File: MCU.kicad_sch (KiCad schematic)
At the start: 12 parts, among them J1 Conn_ARM_SWD_TagConnect_TC203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, SW1 SW_000001, SW2 SW_000001, U1 NORA-B106-00B, Y1 CLK_0003

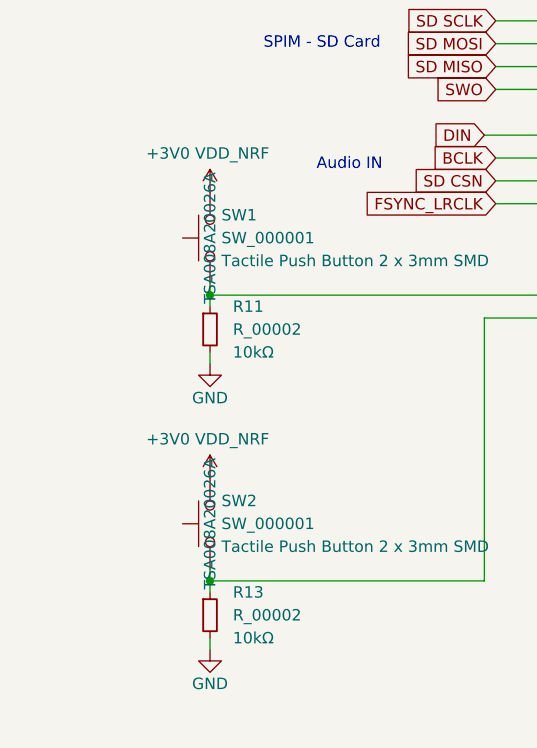
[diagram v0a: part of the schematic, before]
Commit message: fixed SD card footprintg
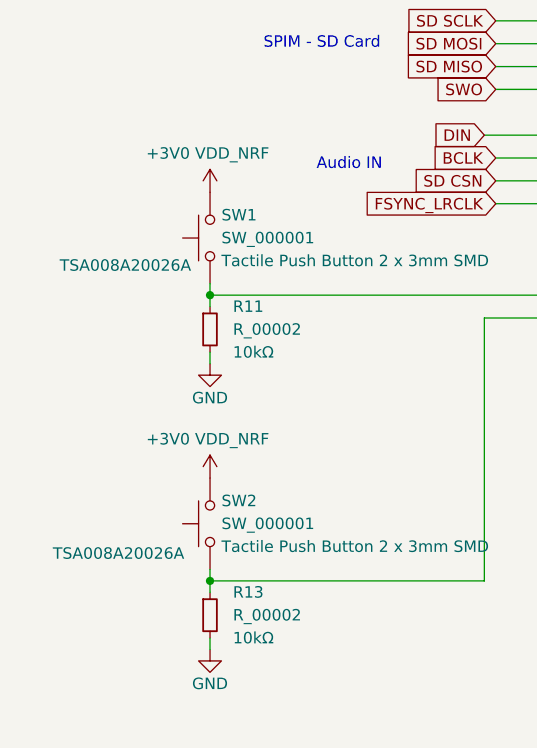
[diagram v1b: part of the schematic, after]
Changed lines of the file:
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@@
 		(on_board yes)
 		(dnp no)
-		(fields_autoplaced yes)
 		(property "Reference" "SW1"
 			(at 49.53 120.6499 90)
@@
 		)
 		(property "MPNs" "TSA008A20026A "
-			(at 48.26 123.19 0)
+			(at 38.862 126.238 90)
 			(effects
 				(font
@@
 		(on_board yes)
 		(dnp no)
-		(fields_autoplaced yes)
 		(property "Reference" "SW2"
 			(at 49.53 152.3999 90)
@@
 		)
 		(property "MPNs" "TSA008A20026A "
-			(at 48.26 154.94 0)
-			(effects
-				(font
+			(at 38.1 158.242 90)
+			(effects
+				(font

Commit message: added test points
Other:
- note removed: "Debug Voltage level Considerations!"
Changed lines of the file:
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@@
-		)
-	)
-	(text "Debug Voltage level Considerations!"
-		(exclude_from_sim no)
-		(at 48.26 21.082 0)
-		(effects
-			(font
-				(size 1.27 1.27)
-			)
 		)
 	)

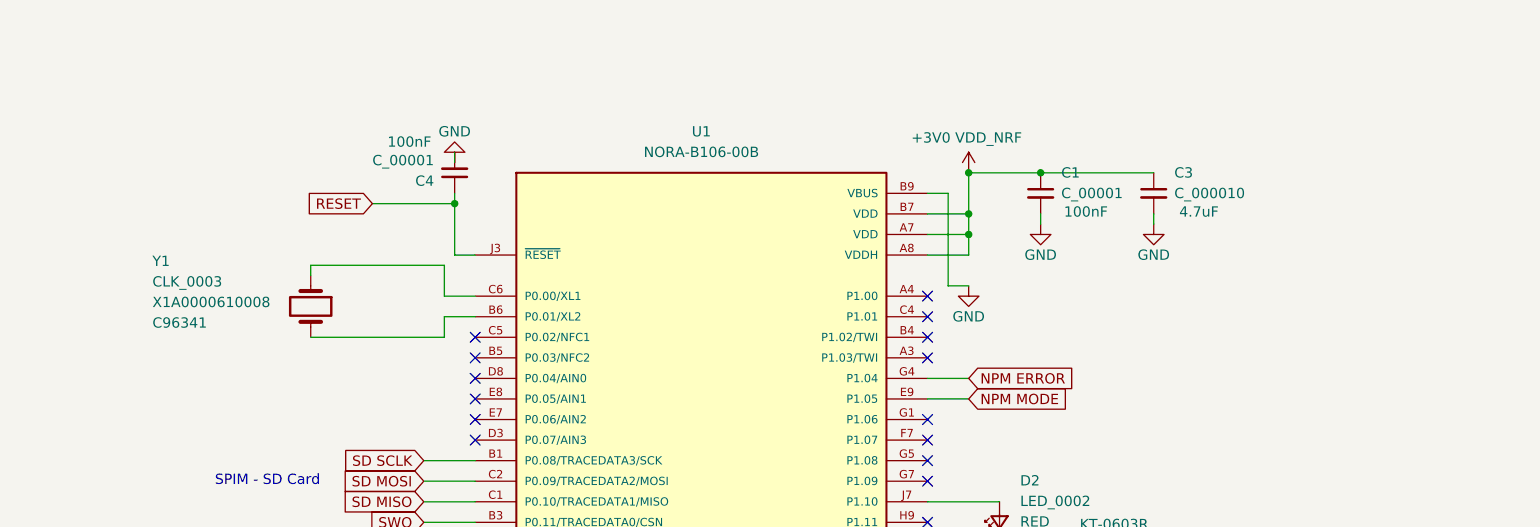
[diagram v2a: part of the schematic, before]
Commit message: added additional decoupling capacitors
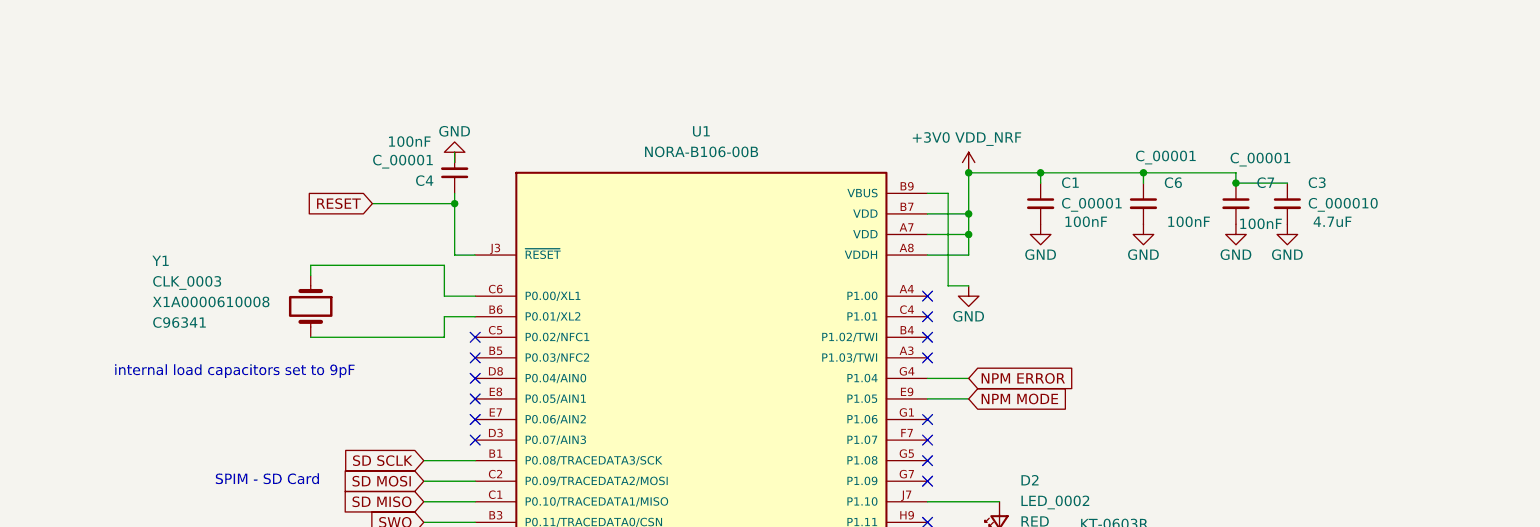
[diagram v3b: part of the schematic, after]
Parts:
- added C6, C7: C_00001, Capacitor_SMD:C_0402_1005Metric, symbol mic_patch_parts:C_00001
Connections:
- net +3V0 VDD_NRF: now also C6.1, C7.1
- net GND: now also C6.2, C7.2
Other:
- note added: "internal load capacitors set to 9pF"
- moved on the sheet: C1, C3

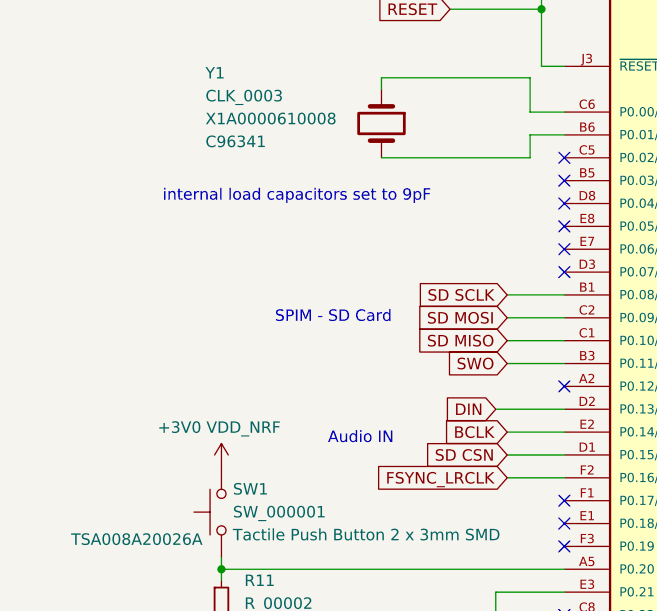
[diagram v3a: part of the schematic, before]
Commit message: fixed ERC errors
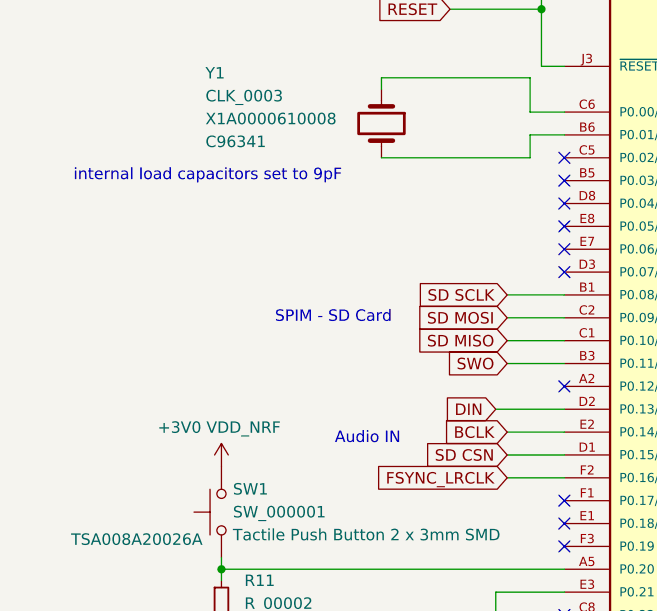
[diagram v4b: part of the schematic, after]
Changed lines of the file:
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@@
 	(text "internal load capacitors set to 9pF"
 		(exclude_from_sim no)
-		(at 56.642 88.138 0)
+		(at 46.736 85.852 0)
 		(effects
 			(font
@@
 	(text "Audio IN"
 		(exclude_from_sim no)
-		(at 63.754 115.062 0)
+		(at 64.516 115.062 0)
 		(effects
 			(font

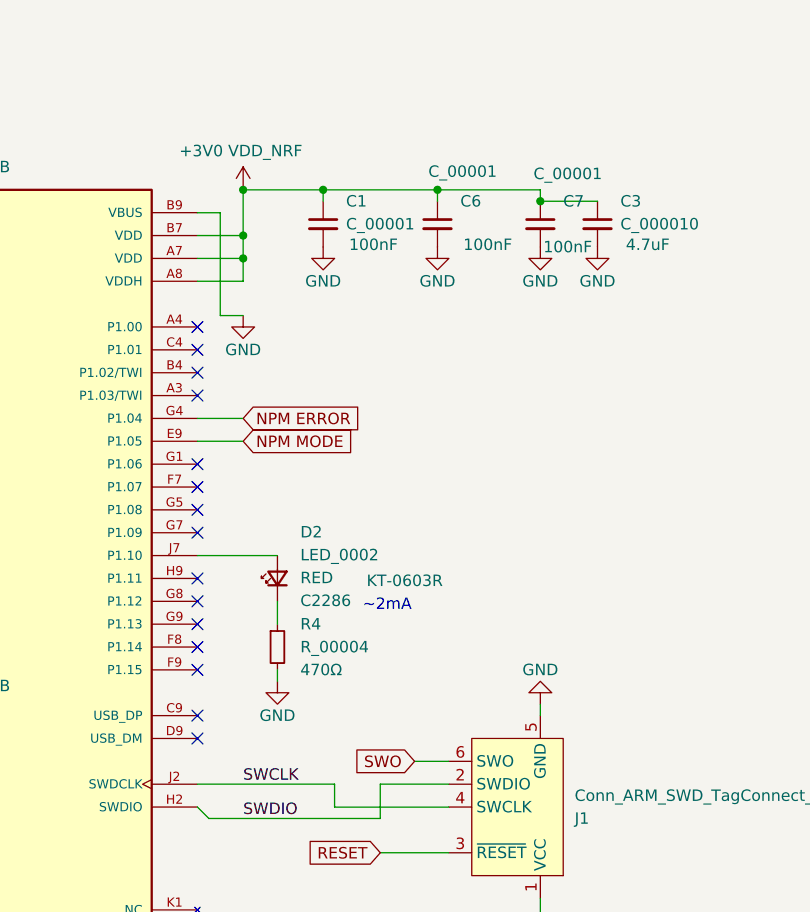
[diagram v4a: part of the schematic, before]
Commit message: switched around pins for easier routing
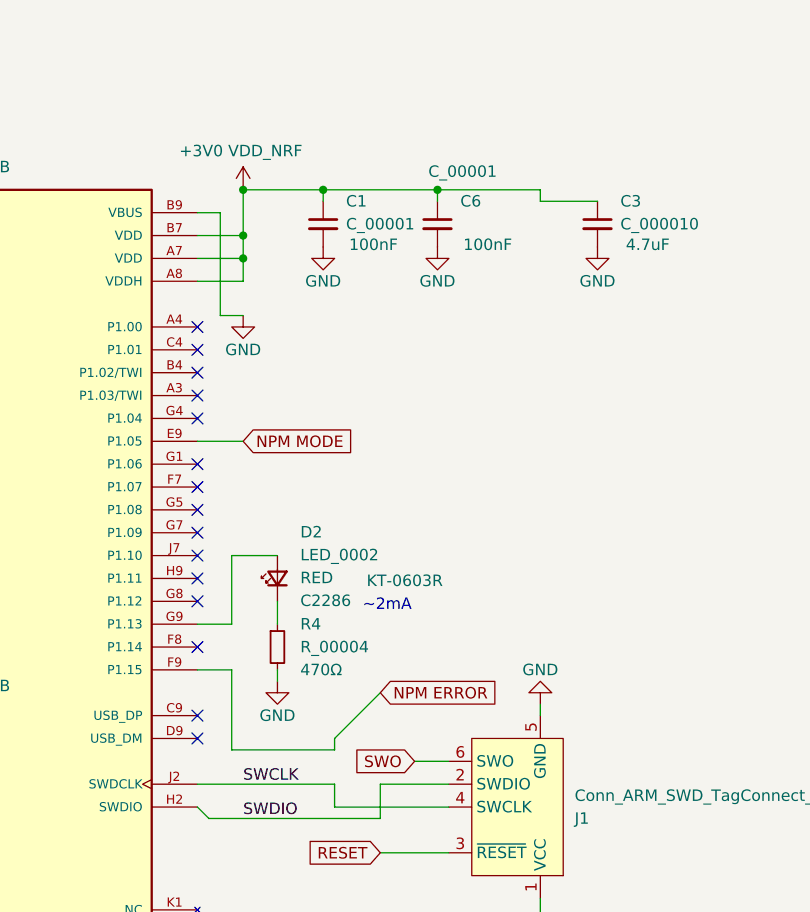
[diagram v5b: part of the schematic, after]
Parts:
- removed C7: C_00001, Capacitor_SMD:C_0402_1005Metric, symbol mic_patch_parts:C_00001
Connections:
- net NPM ERROR: now also U1.F9 (P1.15); no longer U1.G4 (P1.04)
- net at D2.2 (A): now also U1.G9 (P1.13); no longer U1.J7 (P1.10)
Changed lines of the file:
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@@
 	)
 	(junction
-		(at 180.34 64.77)
-		(diameter 0)
-		(color 0 0 0 0)
-	)
-	(junction
 		(at 123.19 170.18)
 		(diameter 0)
@@
 	)
 	(no_connect
-		(at 86.36 124.46)
+		(at 142.24 104.14)
 	)
 	(no_connect
-		(at 142.24 116.84)
+		(at 86.36 124.46)
 	)
 	(no_connect
@@
 	)
 	(no_connect
-		(at 142.24 81.28)
+		(at 142.24 88.9)
 	)
 	(no_connect
-		(at 142.24 111.76)
+		(at 142.24 81.28)
 	)
 	(no_connect
@@
 	(wire
 		(pts
+			(xy 146.05 104.14) (xy 151.13 104.14)
+		)
+		(stroke
+			(width 0)
+			(type default)
+		)
+	)
+	(wire
+		(pts
 			(xy 142.24 129.54) (xy 157.48 129.54)
 		)
@@
 	(wire
 		(pts
+			(xy 146.05 116.84) (xy 146.05 125.73)
+		)
+		(stroke
+			(width 0)
+			(type default)
+		)
+	)
+	(wire
+		(pts
+			(xy 142.24 111.76) (xy 146.05 111.76)
+		)
+		(stroke
+			(width 0)
+			(type default)
+		)
+	)
+	(wire
+		(pts
 			(xy 143.51 133.35) (xy 142.24 132.08)
 		)
@@
 	(wire
 		(pts
+			(xy 142.24 116.84) (xy 146.05 116.84)
+		)
+		(stroke
+			(width 0)
+			(type default)
+		)
+	)
+	(wire
+		(pts
 			(xy 106.68 170.18) (xy 109.22 170.18)
 		)
@@
 	(wire
 		(pts
-			(xy 48.26 160.02) (xy 48.26 161.29)
+			(xy 146.05 104.14) (xy 146.05 111.76)
 		)
 		(stroke
@@
 	(wire
 		(pts
-			(xy 162.56 129.54) (xy 162.56 133.35)
+			(xy 48.26 160.02) (xy 48.26 161.29)
 		)
 		(stroke
@@
 	(wire
 		(pts
-			(xy 48.26 161.29) (xy 48.26 162.56)
+			(xy 162.56 129.54) (xy 162.56 133.35)
 		)
 		(stroke
@@
 	(wire
 		(pts
-			(xy 142.24 104.14) (xy 151.13 104.14)
+			(xy 48.26 161.29) (xy 48.26 162.56)
 		)
 		(stroke
@@
 	(wire
 		(pts
-			(xy 142.24 88.9) (xy 147.32 88.9)
-		)
-		(stroke
-			(width 0)
-			(type default)
-		)
-	)
-	(wire
-		(pts
 			(xy 142.24 91.44) (xy 147.32 91.44)
 		)
@@
 	(wire
 		(pts
+			(xy 157.48 125.73) (xy 157.48 124.46)
+		)
+		(stroke
+			(width 0)
+			(type default)
+		)
+	)
+	(wire
+		(pts
 			(xy 135.89 170.18) (xy 135.89 172.72)
 		)
@@
 	(wire
 		(pts
+			(xy 146.05 125.73) (xy 157.48 125.73)
+		)
+		(stroke
+			(width 0)
+			(type default)
+		)
+	)
+	(wire
+		(pts
 			(xy 91.44 170.18) (xy 93.98 170.18)
 		)
@@
 	(wire
 		(pts
+			(xy 157.48 124.46) (xy 162.56 119.38)
+		)
+		(stroke
+			(width 0)
+			(type default)
+		)
+	)
+	(wire
+		(pts
 			(xy 80.01 114.3) (xy 86.36 114.3)
 		)
@@
 	(global_label "NPM ERROR"
 		(shape input)
-		(at 147.32 88.9 0)
+		(at 162.56 119.38 0)
 		(fields_autoplaced yes)
 		(effects
@@
 		)
 		(property "Intersheetrefs" "${INTERSHEET_REFS}"
-			(at 161.6142 88.9 0)
+			(at 176.8542 119.38 0)
 			(effects
 				(font
@@
 	(symbol
 		(lib_id "mic_patch_parts:C_00001")
-		(at 180.34 67.31 0)
-		(unit 1)
-		(exclude_from_sim no)
-		(in_bom yes)
-		(on_board yes)
-		(dnp no)
-		(property "Reference" "C7"
-			(at 182.88 64.77 0)
-			(do_not_autoplace yes)
-			(effects
-				(font
-					(size 1.27 1.27)
-				)
-				(justify left)
-			)
-		)
-		(property "Value" "C_00001"
-			(at 179.578 61.722 0)
-			(do_not_autoplace yes)
-			(effects
-				(font
-					(size 1.27 1.27)
-				)
-				(justify left)
-			)
-		)
-		(property "Footprint" "Capacitor_SMD:C_0402_1005Metric"
-			(at 154.94 68.58 0)
-			(effects
-				(font
-					(size 1.27 1.27)
-				)
-				(hide yes)
-			)
-		)
-		(property "Datasheet" "~"
-			(at 180.34 67.31 0)
-			(effects
-				(font
-					(size 1.27 1.27)
-				)
-				(hide yes)
-			)
-		)
-		(property "Description" "100nF"
-			(at 183.388 69.85 0)
-			(do_not_autoplace yes)
-			(effects
-				(font
-					(size 1.27 1.27)
-				)
-			)
-		)
-		(property "Desc" ""
-			(at 182.88 69.85 0)
-			(do_not_autoplace yes)
-			(effects
-				(font
-					(size 1.27 1.27)
-				)
-				(justify left)
-			)
-		)
-		(property "MPNs" "0402WGF1002TCE"
-			(at 158.75 59.69 0)
-			(effects
-				(font
-					(size 1.27 1.27)
-				)
-				(hide yes)
-			)
-		)
-		(property "LCSC PNs" "C25744"
-			(at 160.02 64.77 0)
-			(effects
-				(font
-					(size 1.27 1.27)
-				)
-				(hide yes)
-			)
-		)
-		(pin "1"
-		)
-		(pin "2"
-		)
-		(instances
-			(project "mic_patch_v1"
-				(path "/5448a297-4261-40a5-8009-47199bfe22cb/1e8f7a85-c9d9-4dea-908a-5a79456d7ca4"
-					(reference "C7")
-					(unit 1)
-				)
-			)
-		)
-	)
-	(symbol
-		(lib_id "mic_patch_parts:C_00001")
 		(at 83.82 63.5 180)
 		(unit 1)
@@
 					(unit 1)
 				)
-			)
-		)
-	)
-	(symbol
-		(lib_id "power:GND")
-		(at 180.34 69.85 0)
-		(unit 1)
-		(exclude_from_sim no)
-		(in_bom yes)
-		(on_board yes)
-		(dnp no)
-		(property "Reference" "#PWR021"
-			(at 180.34 76.2 0)
-			(effects
-				(font
-					(size 1.27 1.27)
-				)
-				(hide yes)
-			)
-		)
-		(property "Value" "GND"
-			(at 180.34 73.66 0)
-			(effects
-				(font
-					(size 1.27 1.27)
-				)
-			)
-		)
-		(property "Footprint" ""
-			(at 180.34 69.85 0)
-			(effects
-				(font
-					(size 1.27 1.27)
-				)
-				(hide yes)
-			)
-		)
-		(property "Datasheet" ""
-			(at 180.34 69.85 0)
-			(effects
-				(font
-					(size 1.27 1.27)
-				)
-				(hide yes)
-			)
-		)
-		(property "Description" "Power symbol creates a global label with name \"GND\" , ground"
-			(at 180.34 69.85 0)
-			(effects
-				(font
-					(size 1.27 1.27)
-				)
-				(hide yes)
-			)
-		)
-		(pin "1"
-		)
-		(instances
-			(project "mic_patch_v1"
-				(path "/5448a297-4261-40a5-8009-47199bfe22cb/1e8f7a85-c9d9-4dea-908a-5a79456d7ca4"
-					(reference "#PWR021")
-					(unit 1)
-				)

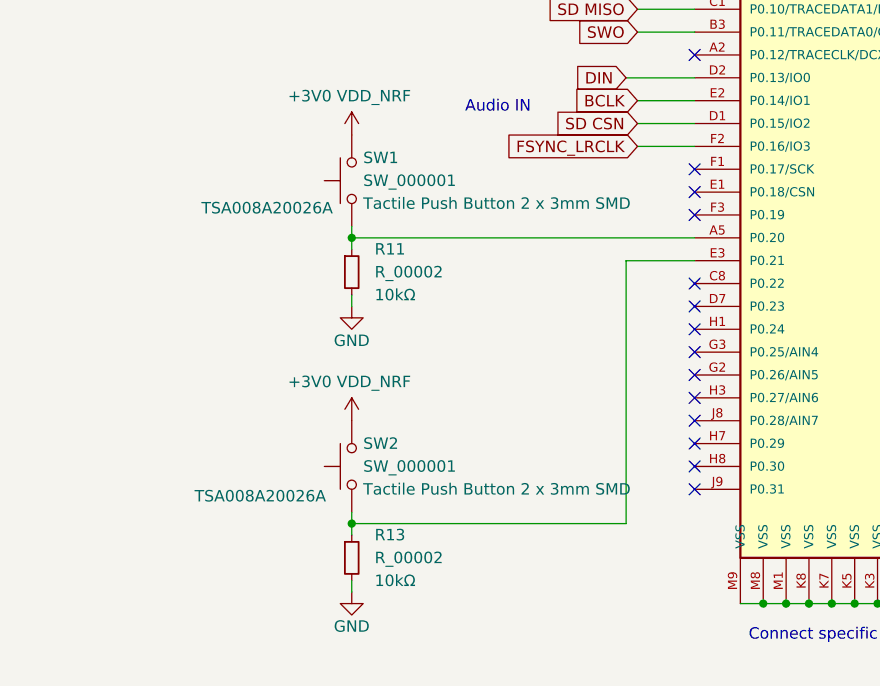
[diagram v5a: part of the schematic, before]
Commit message: re-routed buttons to closer pins
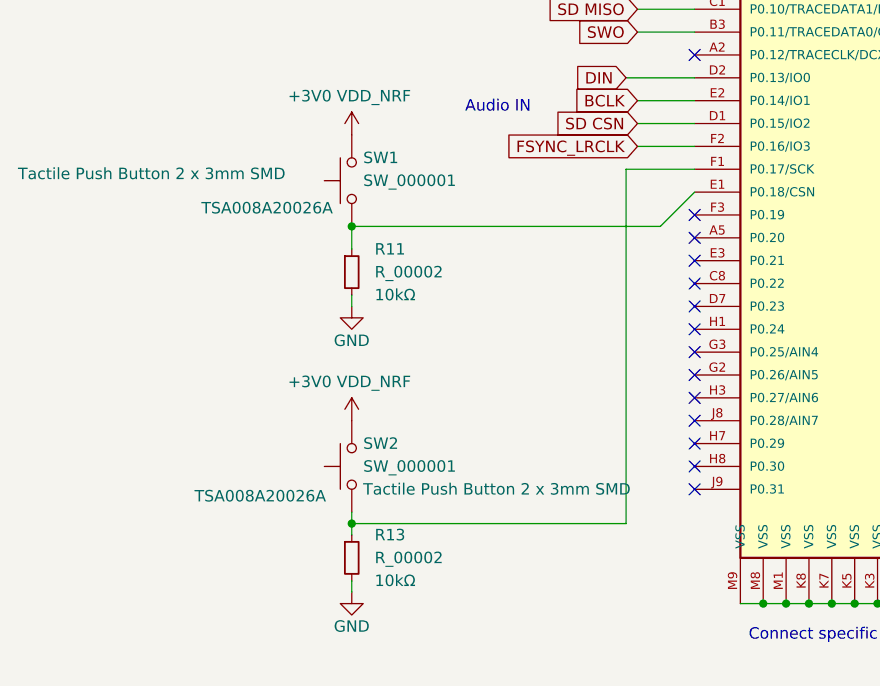
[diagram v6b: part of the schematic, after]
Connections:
- net at R11.1, SW1.1: now also U1.E1 (P0.18/CSN); no longer U1.A5 (P0.20)
- net at R13.1, SW2.1: now also U1.F1 (P0.17/SCK); no longer U1.E3 (P0.21)
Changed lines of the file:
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@@
+	)
+	(junction
+		(at 48.26 128.27)
+		(diameter 0)
+		(color 0 0 0 0)
 	)
 	(junction
@@
 	)
 	(junction
-		(at 48.26 129.54)
-		(diameter 0)
-		(color 0 0 0 0)
-	)
-	(junction
 		(at 110.49 170.18)
 		(diameter 0)
@@
 	)
 	(no_connect
+		(at 86.36 129.54)
+	)
+	(no_connect
 		(at 142.24 104.14)
 	)
 	(no_connect
-		(at 86.36 124.46)
-	)
-	(no_connect
-		(at 86.36 121.92)
-	)
-	(no_connect
 		(at 142.24 96.52)
 	)
@@
 	)
 	(no_connect
+		(at 86.36 132.08)
+	)
+	(no_connect
 		(at 86.36 88.9)
 	)
@@
 	(wire
 		(pts
-			(xy 78.74 132.08) (xy 78.74 161.29)
+			(xy 78.74 121.92) (xy 78.74 161.29)
+		)
+		(stroke
+			(width 0)
+			(type default)
+		)
+	)
+	(wire
+		(pts
+			(xy 82.55 128.27) (xy 86.36 124.46)
 		)
 		(stroke
@@
 	(wire
 		(pts
-			(xy 48.26 128.27) (xy 48.26 129.54)
-		)
-		(stroke
-			(width 0)
-			(type default)
-		)
-	)
-	(wire
-		(pts
 			(xy 146.05 104.14) (xy 151.13 104.14)
 		)
@@
 	(wire
 		(pts
-			(xy 48.26 129.54) (xy 86.36 129.54)
-		)
-		(stroke
-			(width 0)
-			(type default)
-		)
-	)
-	(wire
-		(pts
 			(xy 83.82 60.96) (xy 83.82 62.23)
 		)
@@
 	(wire
 		(pts
-			(xy 78.74 132.08) (xy 86.36 132.08)
-		)
-		(stroke
-			(width 0)
-			(type default)
-		)
-	)
-	(wire
-		(pts
 			(xy 157.48 125.73) (xy 157.48 124.46)
 		)
@@
 	(wire
 		(pts
+			(xy 78.74 121.92) (xy 86.36 121.92)
+		)
+		(stroke
+			(width 0)
+			(type default)
+		)
+	)
+	(wire
+		(pts
 			(xy 135.89 170.18) (xy 135.89 172.72)
 		)
@@
 	(wire
 		(pts
+			(xy 48.26 128.27) (xy 82.55 128.27)
+		)
+		(stroke
+			(width 0)
+			(type default)
+		)
+	)
+	(wire
+		(pts
 			(xy 125.73 170.18) (xy 128.27 170.18)
 		)
@@
 	(wire
 		(pts
-			(xy 48.26 129.54) (xy 48.26 130.81)
+			(xy 48.26 128.27) (xy 48.26 130.81)
 		)
 		(stroke
@@
 		)
 		(property "Desc" "Tactile Push Button 2 x 3mm SMD"
-			(at 49.53 125.7299 90)
-			(effects
-				(font
+			(at 11.176 122.428 90)
+			(effects
+				(font
